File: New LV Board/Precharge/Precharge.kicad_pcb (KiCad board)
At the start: 2 copper layers, 12 parts, among them J1 Conn_01x07, Q1 DMN3404L, U1 LM324, U2 Optocoupler

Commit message: Precharge work
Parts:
- removed J1: Conn_01x07, Connector_JST:JST_EH_B7B-EH-A_1x07_P2.50mm_Vertical
- removed R3: 100k, Resistor_THT:R_Axial_DIN0411_L9.9mm_D3.6mm_P7.62mm_Vertical
- removed U2: Optocoupler, Package_SO:SOIC-4_4.55x3.7mm_P2.54mm
- added C1: 47u, Capacitor_SMD:C_1210_3225Metric_Pad1.33x2.70mm_HandSolder, F.Cu at (88.3, 36.8)
- added C3: 0.1u, Capacitor_SMD:C_1206_3216Metric_Pad1.33x1.80mm_HandSolder, F.Cu at (83.8, 36.8)
- added C6: 1u, Capacitor_SMD:C_1206_3216Metric_Pad1.33x1.80mm_HandSolder, F.Cu at (58.4, 39.4)
- added C7: 0.1u, Capacitor_SMD:C_1206_3216Metric_Pad1.33x1.80mm_HandSolder, F.Cu at (58.4, 31.8)
- added K1: G3VM-61G2, Precharge:G-SOP4_OMR, F.Cu at (68.7, 37.5)
- added Q2: MPSA42, Package_TO_SOT_THT:TO-92, F.Cu at (90.2, 24.1)
- added Q4: IRLML5203, Package_TO_SOT_SMD:SOT-23_Handsoldering, F.Cu at (78.7, 37.5)
- added R10: 10k, Resistor_THT:R_Axial_DIN0207_L6.3mm_D2.5mm_P2.54mm_Vertical, F.Cu at (92.1, 37.9)
- added R11: 100k, Resistor_THT:R_Axial_DIN0516_L15.5mm_D5.0mm_P7.62mm_Vertical, F.Cu at (45.7, 33.0)
- added R12: 100k, Resistor_THT:R_Axial_DIN0516_L15.5mm_D5.0mm_P7.62mm_Vertical, F.Cu at (45.7, 38.7)
- added R13: 2k, Resistor_THT:R_Axial_DIN0207_L6.3mm_D2.5mm_P2.54mm_Vertical, F.Cu at (33.6, 24.1)
- added R14: 22k, Resistor_THT:R_Axial_DIN0207_L6.3mm_D2.5mm_P2.54mm_Vertical, F.Cu at (63.5, 37.7)
- added R15: 2.2k, Resistor_THT:R_Axial_DIN0207_L6.3mm_D2.5mm_P2.54mm_Vertical, F.Cu at (67.3, 32.0)
- added R16: 220, Resistor_THT:R_Axial_DIN0207_L6.3mm_D2.5mm_P2.54mm_Vertical, F.Cu at (63.5, 32.0)
- added R9: 57.6k, Resistor_THT:R_Axial_DIN0207_L6.3mm_D2.5mm_P2.54mm_Vertical, F.Cu at (90.2, 28.6)
- added U3: NE555P, Package_DIP:DIP-8_W7.62mm, F.Cu at (78.7, 22.9)
- added U4: LR8N3-G, Package_TO_SOT_THT:TO-92, F.Cu at (57.1, 35.9)
- Q1: value DMN3404L -> BSS214NW; footprint Package_TO_SOT_SMD:SOT-23-3 -> Package_TO_SOT_SMD:SOT-323_SC-70_Handsoldering
- R1: value 1M -> 100k; footprint Resistor_THT:R_Axial_DIN0411_L9.9mm_D3.6mm_P7.62mm_Vertical -> Resistor_THT:R_Axial_DIN0516_L15.5mm_D5.0mm_P5.08mm_Vertical
- R2: value 10k -> 100k; footprint Resistor_THT:R_Axial_DIN0411_L9.9mm_D3.6mm_P7.62mm_Vertical -> Resistor_THT:R_Axial_DIN0516_L15.5mm_D5.0mm_P5.08mm_Vertical
- R4: value 5k -> 22k; footprint Resistor_THT:R_Axial_DIN0411_L9.9mm_D3.6mm_P7.62mm_Vertical -> Resistor_THT:R_Axial_DIN0207_L6.3mm_D2.5mm_P2.54mm_Vertical
- R5: value 1M -> 100k; footprint Resistor_THT:R_Axial_DIN0411_L9.9mm_D3.6mm_P7.62mm_Vertical -> Resistor_THT:R_Axial_DIN0207_L6.3mm_D2.5mm_P2.54mm_Vertical
- R6: value 22k -> 100k; footprint Resistor_THT:R_Axial_DIN0411_L9.9mm_D3.6mm_P7.62mm_Vertical -> Resistor_THT:R_Axial_DIN0207_L6.3mm_D2.5mm_P2.54mm_Vertical
- R7: footprint Resistor_THT:R_Axial_DIN0411_L9.9mm_D3.6mm_P7.62mm_Vertical -> Resistor_THT:R_Axial_DIN0516_L15.5mm_D5.0mm_P5.08mm_Vertical
- R8: value 22k -> 100k; footprint Resistor_THT:R_Axial_DIN0411_L9.9mm_D3.6mm_P7.62mm_Vertical -> Resistor_THT:R_Axial_DIN0516_L15.5mm_D5.0mm_P5.08mm_Vertical
- U1: value LM324 -> LM2904; footprint Package_DIP:CERDIP-14_W7.62mm_SideBrazed -> Package_DIP:DIP-8_W7.62mm
- moved R7 222.6 mm to (29.2, 29.2), turned to 90 degrees
- moved R8 190.8 mm to (29.2, 38.7), turned to 90 degrees
- moved R6 182.7 mm to (54.0, 24.1), turned to 0 degrees
- moved R4 179.7 mm to (43.2, 24.1), turned to 0 degrees
- moved Q1 176.6 mm to (91.4, 32.4), turned to 180 degrees
- moved R5 174.4 mm to (48.5, 24.1), turned to 0 degrees
- moved U1 170.6 mm to (67.3, 21.6), turned to -90 degrees
- moved R2 169.3 mm to (38.7, 38.7), turned to 90 degrees
- moved R1 163.5 mm to (38.7, 29.2), turned to 90 degrees
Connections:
- Q1 pad 2: AIR1- -> GLV-
- Q1 pad 3: GLV- -> AIR1-
- R1 pad 1: HVPACK+ -> Net-(R1-Pad1)
- R1 pad 2: Net-(U1A--) -> Net-(R1-Pad2)
- R2 pad 1: Net-(U1A--) -> HVPACK+
- R2 pad 2: HVPACK- -> Net-(R1-Pad1)
- R4 pad 1: Net-(U1E-V-) -> Net-(R1-Pad2)
- R4 pad 2: HVPACK- -> Net-(U1A-+)
- R5 pad 2: TS+ -> Net-(R5-Pad2)
- R6 pad 1: Net-(U1A-+) -> Net-(R5-Pad2)
- R7 pad 1: Done -> Net-(R7-Pad1)
- R7 pad 2: AIR1- -> Net-(U1A--)
- R8 pad 1: Net-(U1A-+) -> TS+
- R8 pad 2: HVPACK- -> Net-(R7-Pad1)
- U1 pad 5: (no net) -> unconnected-(U1B-+-Pad5)
- U1 pad 6: (no net) -> unconnected-(U1B---Pad6)
- U1 pad 7: (no net) -> unconnected-(U1-Pad7)
- U1 pad 8: (no net) -> Net-(U1C-V+)
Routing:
- net HVPACK-: track 104.2 -> 0.00 mm, vias 0 -> 2
- net TS+: track 58.1 -> 0.00 mm
- net HVPACK+: track 66.5 -> 11.4 mm
- net Net-(U1E-V-): track 40.4 -> 0.00 mm
- net Net-(Q2-C): track 0.00 -> 28.9 mm
- net TSMS+: track 17.8 -> 36.1 mm, vias 0 -> 3
- net U43: track 0.00 -> 17.7 mm
- net Net-(U1C-V+): track 0.00 -> 16.5 mm
- net AIR1-: track 28.2 -> 14.4 mm, vias 0 -> 2
- net Net-(U4-IN): track 0.00 -> 13.4 mm
- net Done: track 36.8 -> 23.7 mm
- net Net-(Q4-G): track 0.00 -> 12.2 mm
- net Net-(U1A-+): track 31.2 -> 19.1 mm
- net GLV-: track 12.6 -> 0.75 mm, vias 0 -> 3
- net Net-(U3-CV): track 0.00 -> 5.84 mm
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- added copper zone on B.Cu, net GLV-
- added copper zone on F.Cu, net HVPACK+
- added copper zone on B.Cu, net HVPACK-
- added copper zone on F.Cu, net U43
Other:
- board outline added: 76.2 x 33 mm
- board text added: "${REFERENCE}"

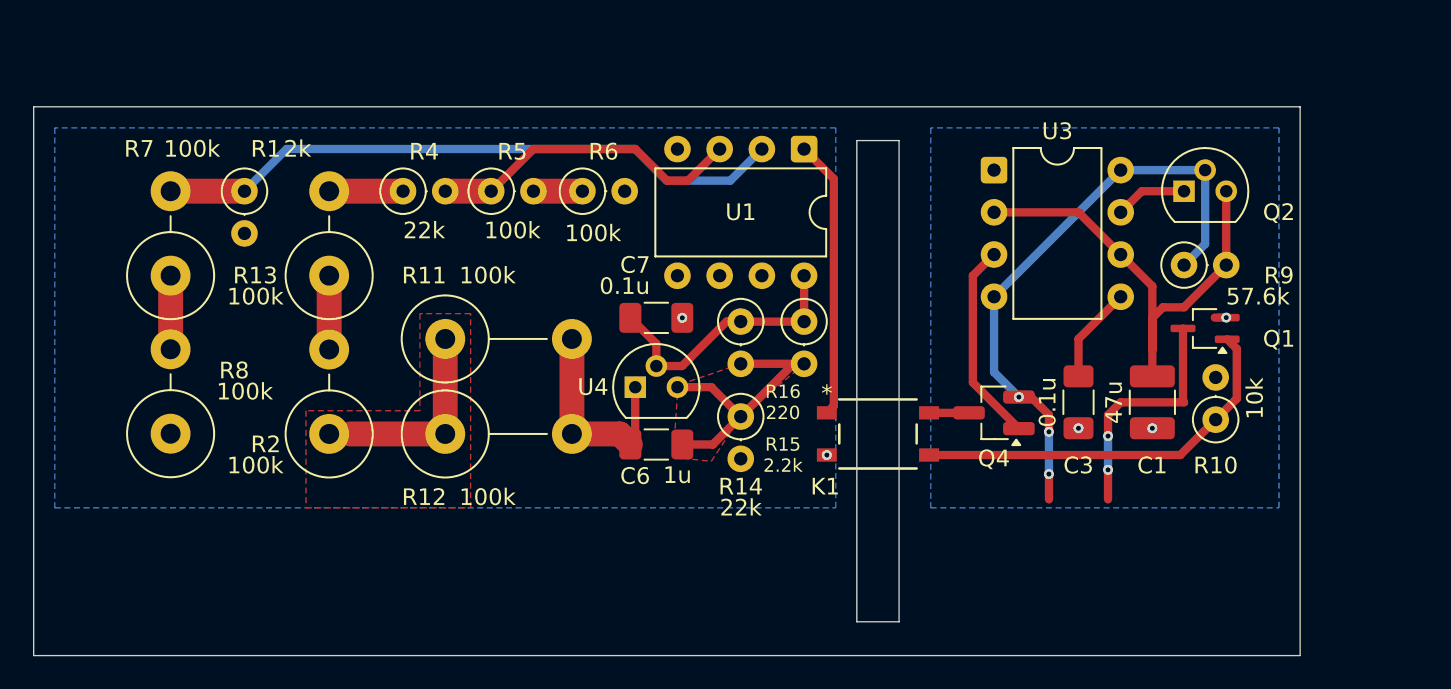
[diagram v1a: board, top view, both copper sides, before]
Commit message: added screw terminals and GLV- trace
Haven't added any screw mount holes yet
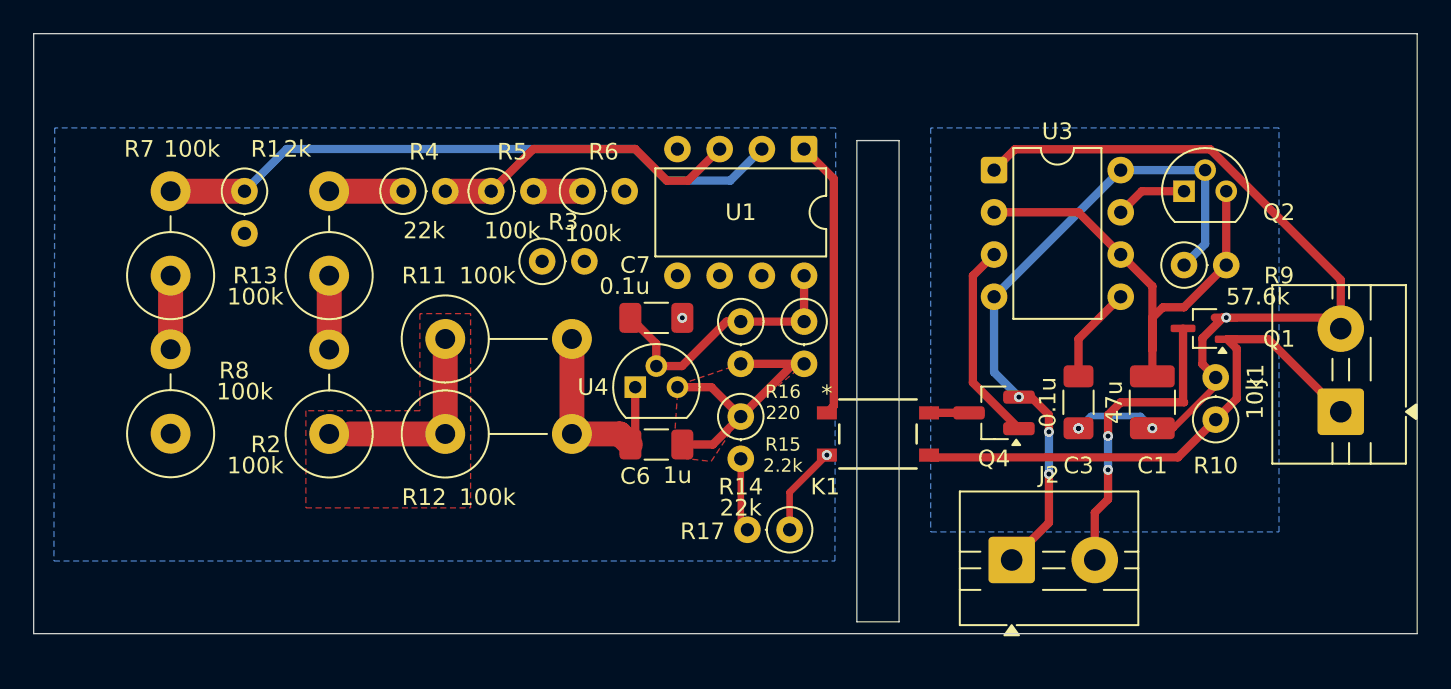
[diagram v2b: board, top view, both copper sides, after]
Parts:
- added J1: Screw_Terminal_01x02, TerminalBlock:TerminalBlock_MaiXu_MX126-5.0-02P_1x02_P5.00mm, F.Cu at (99.6, 37.4)
- added J2: Screw_Terminal_01x02, TerminalBlock:TerminalBlock_MaiXu_MX126-5.0-02P_1x02_P5.00mm, F.Cu at (79.8, 46.3)
- added R17: 5k, Resistor_THT:R_Axial_DIN0207_L6.3mm_D2.5mm_P2.54mm_Vertical, F.Cu at (66.4, 44.5)
- added R3: 2k, Resistor_THT:R_Axial_DIN0207_L6.3mm_D2.5mm_P2.54mm_Vertical, F.Cu at (51.5, 28.4)
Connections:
- net U43 renamed Net-(U4-ADJ)
- K1 pad 2: HVPACK- -> Net-(K1-Pad2)
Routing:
- net GLV-: track 0.75 -> 50.6 mm, vias 3 -> 4
- net Done: track 23.7 -> 32.5 mm
- net Net-(K1-Pad2): track 0.00 -> 5.42 mm, vias 0 -> 1
- net TSMS+: track 36.1 -> 40.7 mm
- net HVPACK-: track 0.00 -> 4.44 mm, vias 2 -> 1
- net AIR1-: track 14.4 -> 18.4 mm
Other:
- board size 76.2 x 33 mm -> 83.2 x 36.1 mm

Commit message: added mounting holes
does HV- need to be traced?
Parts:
- added H1: MountingHole_Pad, MountingHole:MountingHole_5.3mm_M5_DIN965_Pad, F.Cu at (57.0, 48.5)
- added H2: MountingHole_Pad, MountingHole:MountingHole_5.3mm_M5_DIN965_Pad, F.Cu at (45.4, 48.3)
- added H3: MountingHole_Pad, MountingHole:MountingHole_5.3mm_M5_DIN965_Pad, F.Cu at (29.4, 47.8)
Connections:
- J1 pad GLV-: GLV- -> (no net)
- J2 pad 2: AIR1- -> GLV-
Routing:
- net HVPACK+: track 11.4 -> 21.1 mm
- net TS+: track 0.00 -> 9.14 mm
- net HVPACK-: track 4.44 -> 13.0 mm
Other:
- board size 83.2 x 36.1 mm -> 83.2 x 41.2 mm

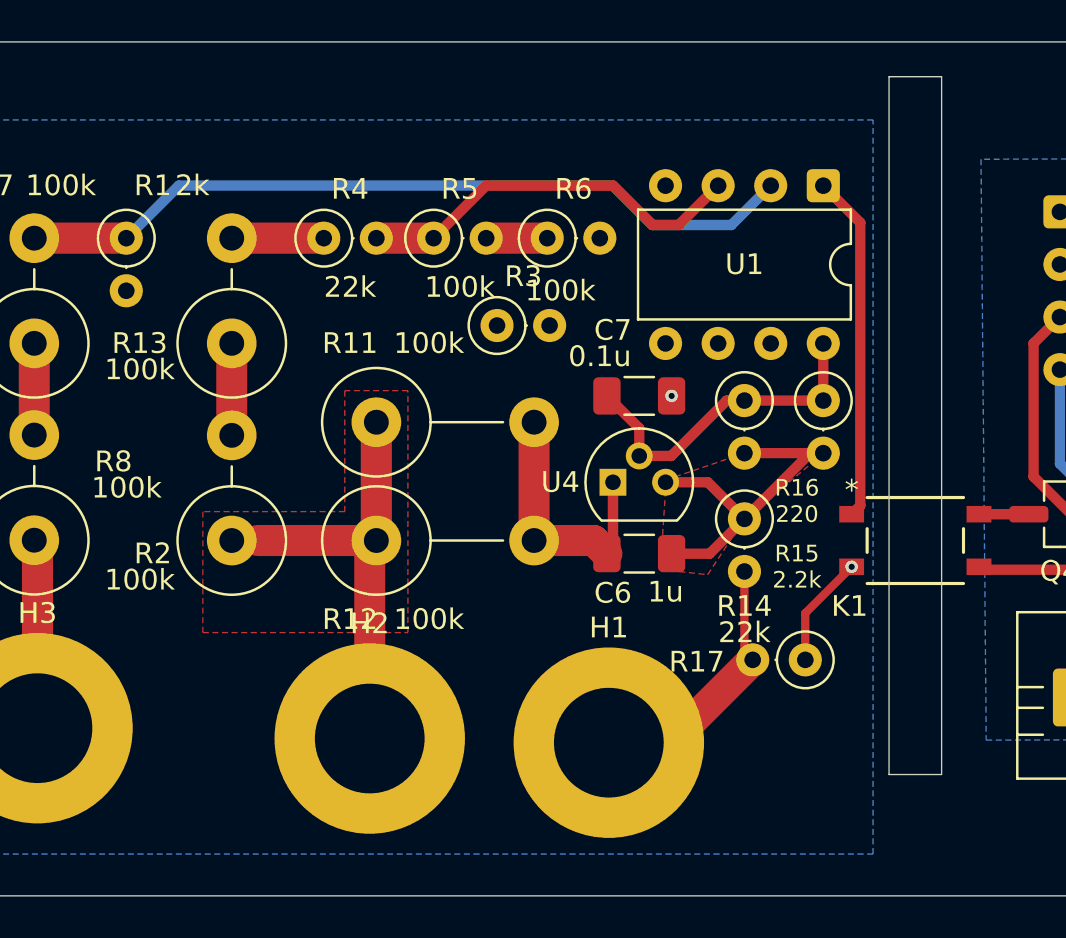
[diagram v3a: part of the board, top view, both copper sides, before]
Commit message: Added HV- Traces
I believe everything is all set
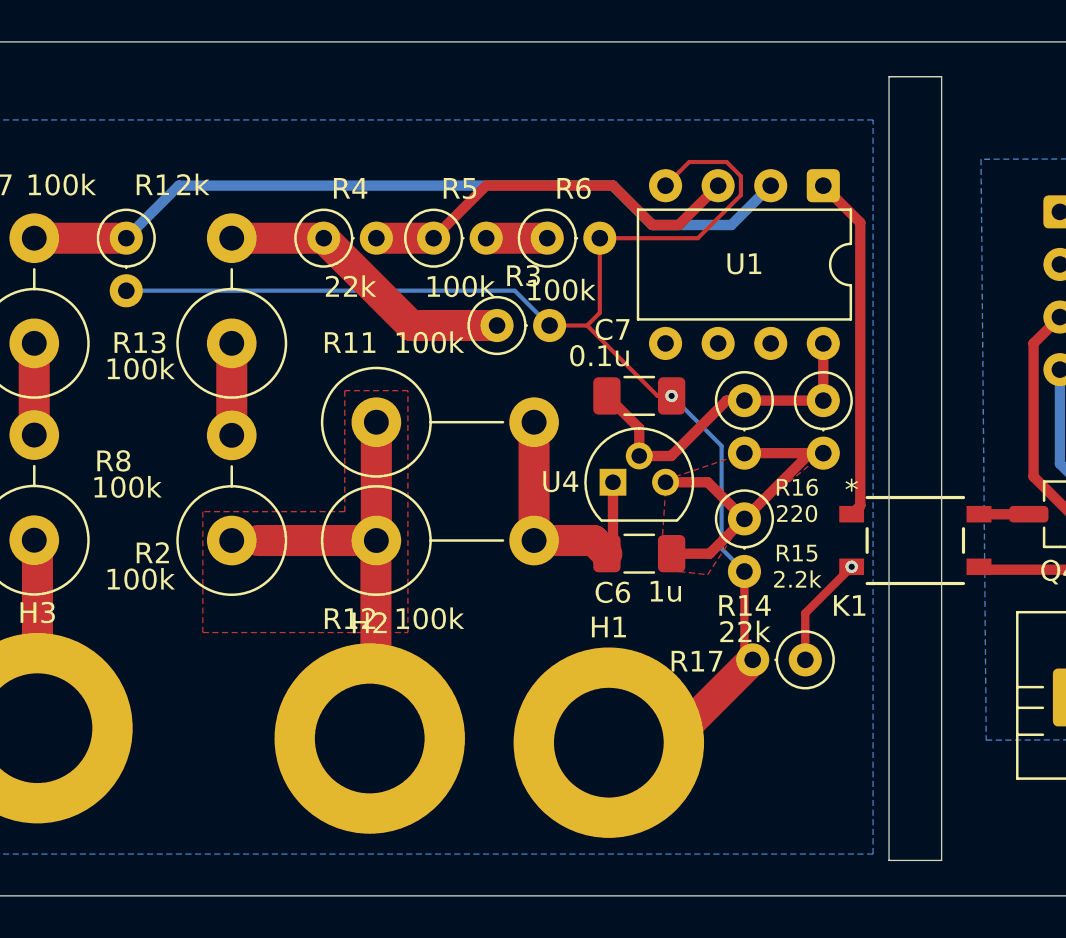
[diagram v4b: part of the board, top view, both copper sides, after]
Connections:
- J2 pad 2: GLV- -> AIR1-
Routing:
- net HVPACK-: track 13.0 -> 68.9 mm
- net Net-(R1-Pad2): track 4.45 -> 14.6 mm
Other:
- outline, holes or cut-outs redrawn
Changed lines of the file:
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@@
 			(layers "*.Cu" "*.Mask")
 			(remove_unused_layers no)
-			(net 9 "GLV-")
+			(net 8 "AIR1-")
 			(pinfunction "Pin_2")
 			(pintype "passive")
@@
 	(gr_rect
 		(start 70.485 16.332)
-		(end 73.025 50.038)
+		(end 73.025 54.188)
 		(stroke
 			(width 0.05)
@@
 	)
 	(segment
+		(start 61.25205 24.13)
+		(end 63.331 22.05105)
+		(width 0.2)
+		(layer "F.Cu")
+		(net 4)
+	)
+	(segment
+		(start 59.3 31.75)
+		(end 59.9825 31.75)
+		(width 0.2)
+		(layer "F.Cu")
+		(net 4)
+	)
+	(segment
 		(start 63.5 40.23)
 		(end 63.5 44.1)
@@
 	)
 	(segment
+		(start 56.515 24.13)
+		(end 61.25205 24.13)
+		(width 0.2)
+		(layer "F.Cu")
+		(net 4)
+	)
+	(segment
 		(start 56.95 48.5)
 		(end 59.9 48.5)
@@
 	)
 	(segment
+		(start 62.64205 20.45)
+		(end 60.835 20.45)
+		(width 0.2)
+		(layer "F.Cu")
+		(net 4)
+	)
+	(segment
+		(start 54.09 28.35)
+		(end 55.9 28.35)
+		(width 0.2)
+		(layer "F.Cu")
+		(net 4)
+	)
+	(segment
+		(start 55.9 28.35)
+		(end 59.3 31.75)
+		(width 0.2)
+		(layer "F.Cu")
+		(net 4)
+	)
+	(segment
+		(start 56.515 27.735)
+		(end 56.515 24.13)
+		(width 0.2)
+		(layer "F.Cu")
+		(net 4)
+	)
+	(segment
+		(start 63.331 22.05105)
+		(end 63.331 21.13895)
+		(width 0.2)
+		(layer "F.Cu")
+		(net 4)
+	)
+	(segment
 		(start 63.5 44.1)
 		(end 63.9 44.5)
@@
 		(net 4)
 	)
+	(segment
+		(start 55.9 28.35)
+		(end 56.515 27.735)
+		(width 0.2)
+		(layer "F.Cu")
+		(net 4)
+	)
+	(segment
+		(start 63.331 21.13895)
+		(end 62.64205 20.45)
+		(width 0.2)
+		(layer "F.Cu")
+		(net 4)
+	)
+	(segment
+		(start 60.835 20.45)
+		(end 59.69 21.595)
+		(width 0.2)
+		(layer "F.Cu")
+		(net 4)
+	)
 	(via
 		(at 59.9825 31.75)
@@
 	)
 	(segment
+		(start 62.399 39.129)
+		(end 63.5 40.23)
+		(width 0.2)
+		(layer "B.Cu")
+		(net 4)
+	)
+	(segment
+		(start 33.64 26.67)
+		(end 52.41 26.67)
+		(width 0.2)
+		(layer "B.Cu")
+		(net 4)
+	)
+	(segment
+		(start 52.41 26.67)
+		(end 54.09 28.35)
+		(width 0.2)
+		(layer "B.Cu")
+		(net 4)
+	)
+	(segment
+		(start 62.399 34.1665)
+		(end 62.399 39.129)
+		(width 0.2)
+		(layer "B.Cu")
+		(net 4)
+	)
+	(segment
+		(start 59.9825 31.75)
+		(end 62.399 34.1665)
+		(width 0.2)
+		(layer "B.Cu")
+		(net 4)
+	)
+	(segment
 		(start 74.83 37.465)
 		(end 77.235 37.465)
@@
 	)
 	(segment
+		(start 43.18 24.13)
+		(end 47.4 28.35)
+		(width 1.5)
+		(layer "F.Cu")
+		(net 14)
+	)
+	(segment
+		(start 47.4 28.35)
+		(end 51.55 28.35)
+		(width 1.5)
+		(layer "F.Cu")
+		(net 14)
+	)
+	(segment
 		(start 38.735 24.13)
 		(end 43.18 24.13)
@@
 	)
 	(segment
-		(start 45.4 39.055)
+		(start 39.99 38.735)
 		(end 45.72 38.735)
 		(width 1.5)
@@
 	)
 	(segment
-		(start 39.99 38.735)
-		(end 45.72 38.735)
+		(start 45.4 48.3)
+		(end 45.7 48)
 		(width 1.5)
 		(layer "F.Cu")
@@
 	)
 	(segment
-		(start 45.4 48.3)
-		(end 45.4 39.055)
+		(start 45.7 48)
+		(end 45.7 38.755)
+		(width 1.5)
+		(layer "F.Cu")
+		(net 15)
+	)
+	(segment
+		(start 45.7 38.755)
+		(end 45.72 38.735)
 		(width 1.5)
 		(layer "F.Cu")
@@
 		(min_thickness 0.2)
 		(filled_areas_thickness no)
-		(fill
+		(fill yes
 			(thermal_gap 0.5)
 			(thermal_bridge_width 0.5)
